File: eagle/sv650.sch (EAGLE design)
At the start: 31 parts, among them Q1 IRLML6344

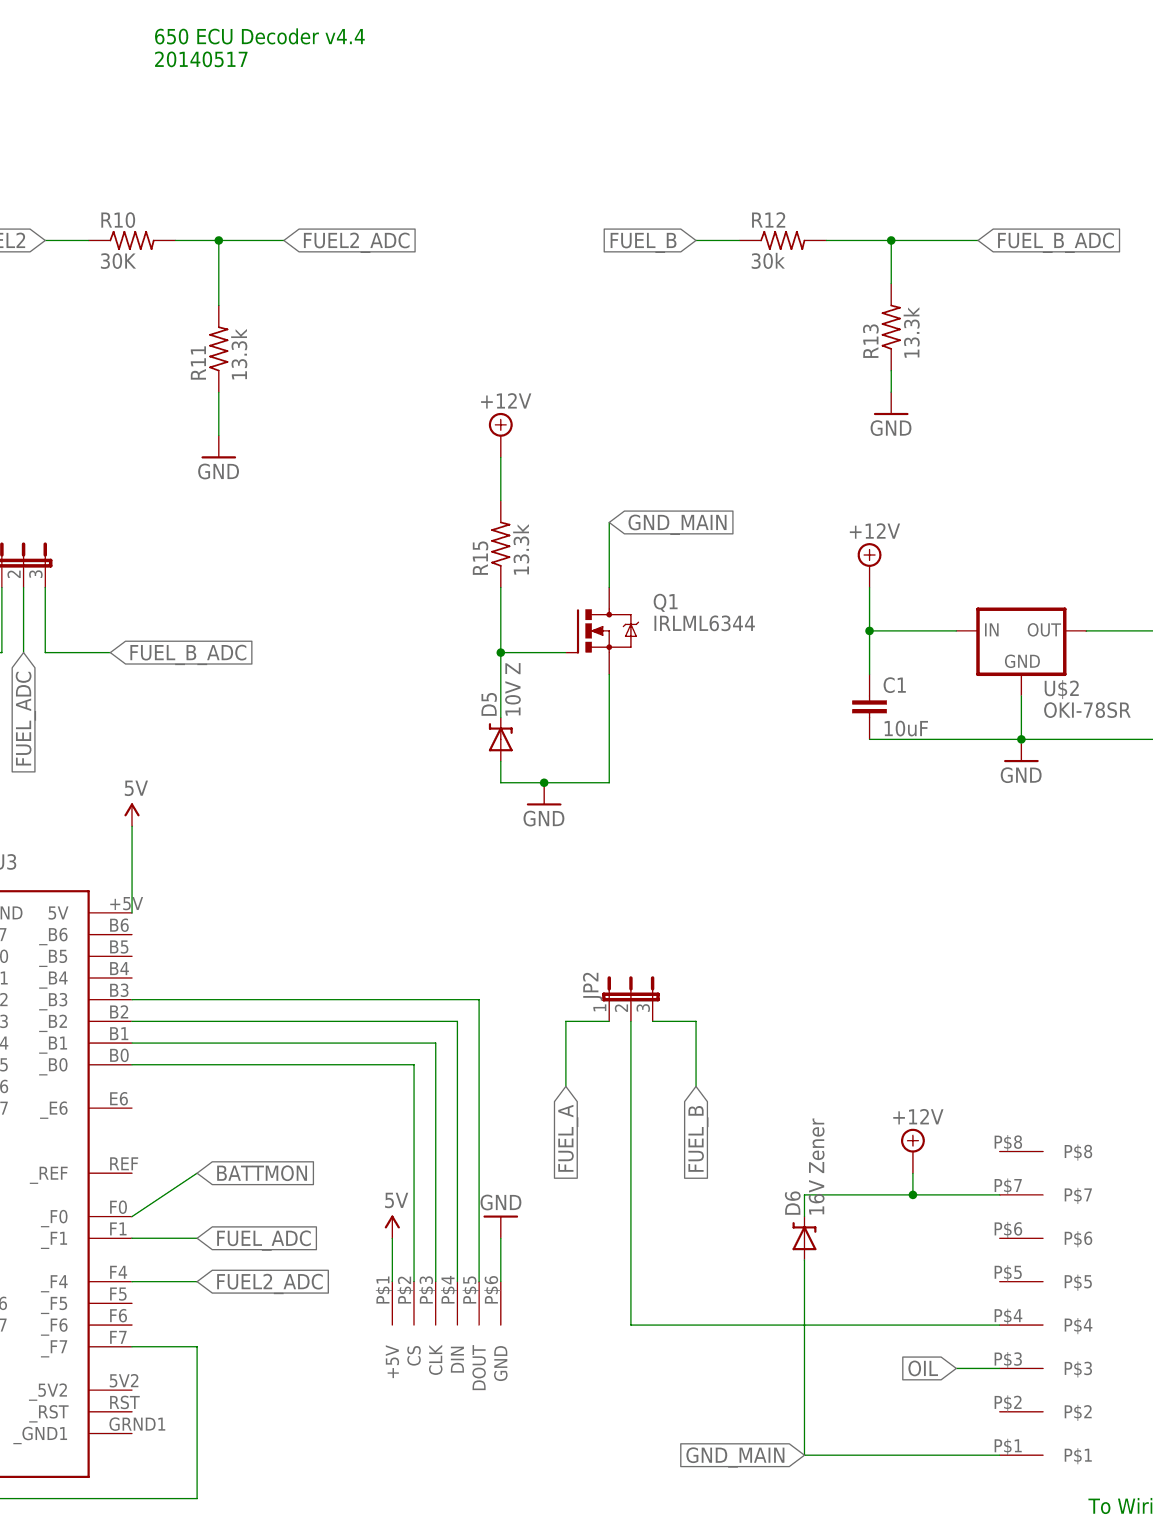
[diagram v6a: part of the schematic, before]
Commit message: replace 16V zener with 15V TVS
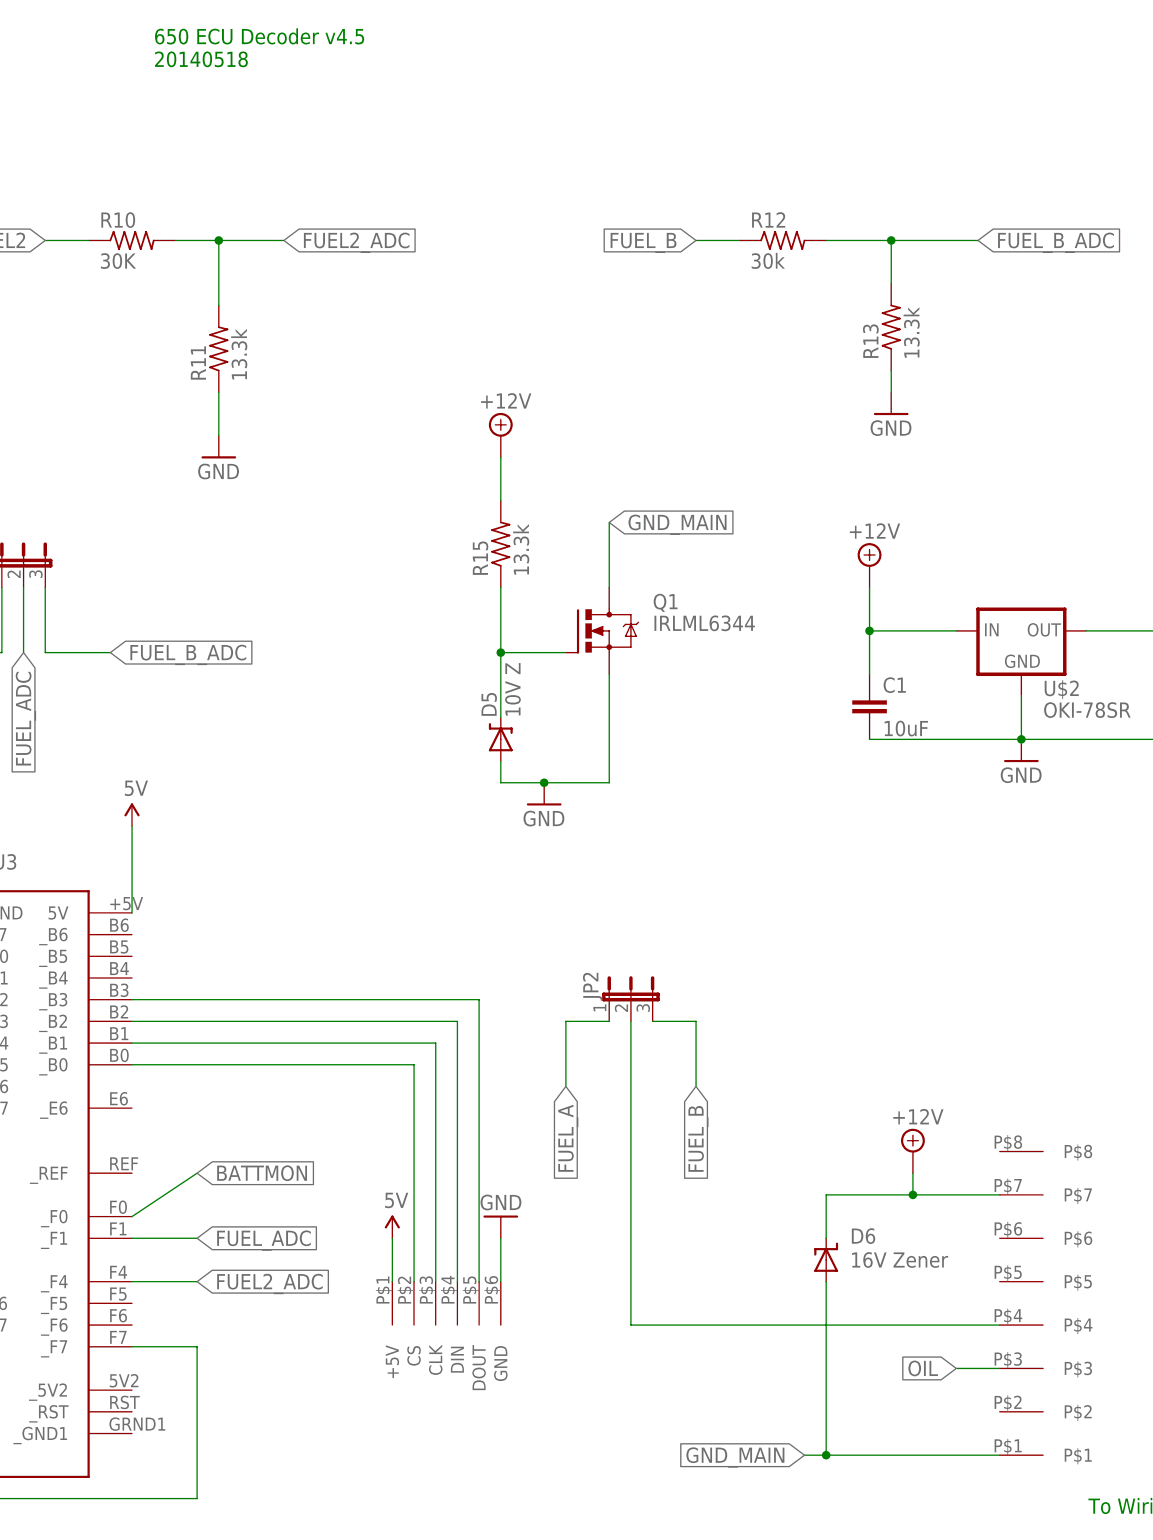
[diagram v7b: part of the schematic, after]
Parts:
- D6: device SparkFun-DiscreteSemi:DIODE-ZENER-BZT52 -> diode:SUPPRESSOR-SMBG
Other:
- note added: "650 ECU Decoder v4.5 20140518"
- note removed: "650 ECU Decoder v4.4 20140517"
- moved on the sheet: D6
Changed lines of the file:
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@@
 <part name="GND8" library="SparkFun" deviceset="GND" device=""/>
 <part name="SUPPLY1" library="supply2" deviceset="+12V" device=""/>
-<part name="D6" library="SparkFun-DiscreteSemi" deviceset="DIODE-ZENER" device="-BZT52" value="16V Zener"/>
+<part name="D6" library="diode" deviceset="SUPPRESSOR-" device="SMBG" value="16V Zener"/>
 <part name="SUPPLY3" library="supply2" deviceset="+12V" device=""/>
 <part name="R5" library="synfinatic" deviceset="RESISTOR" device="PTH-5W" value="82"/>
@@
 <plain>
 <text x="157.48" y="-38.1" size="1.778" layer="91" rot="R180">To Wiring Harness</text>
-<text x="27.94" y="129.54" size="1.778" layer="91">650 ECU Decoder v4.4
-20140517</text>
+<text x="27.94" y="129.54" size="1.778" layer="91">650 ECU Decoder v4.5
+20140518</text>
 </plain>
 <instances>
@@
 <instance part="GND8" gate="1" x="-91.44" y="15.24"/>
 <instance part="SUPPLY1" gate="+12V" x="-43.18" y="76.2"/>
-<instance part="D6" gate="G$1" x="104.14" y="-7.62" rot="R90"/>
+<instance part="D6" gate="G$1" x="106.68" y="-10.16"/>
 <instance part="SUPPLY3" gate="+12V" x="-81.28" y="129.54"/>
 <instance part="R5" gate="G$1" x="-68.58" y="116.84" rot="R90"/>
@@
 <pinref part="SUPPLY4" gate="+12V" pin="+12V"/>
 <wire x1="116.84" y1="0" x2="116.84" y2="-2.54" width="0.1524" layer="91"/>
-<wire x1="116.84" y1="-2.54" x2="104.14" y2="-2.54" width="0.1524" layer="91"/>
+<wire x1="116.84" y1="-2.54" x2="106.68" y2="-2.54" width="0.1524" layer="91"/>
 <junction x="116.84" y="-2.54"/>
-<wire x1="104.14" y1="-2.54" x2="104.14" y2="-5.08" width="0.1524" layer="91"/>
 <pinref part="D6" gate="G$1" pin="C"/>
+<wire x1="106.68" y1="-2.54" x2="106.68" y2="-7.62" width="0.1524" layer="91"/>
 </segment>
 <segment>
@@
 <segment>
 <pinref part="U$3" gate="G$1" pin="P$1"/>
-<wire x1="104.14" y1="-10.16" x2="104.14" y2="-33.02" width="0.1524" layer="91"/>
-<wire x1="104.14" y1="-33.02" x2="127" y2="-33.02" width="0.1524" layer="91"/>
+<wire x1="104.14" y1="-33.02" x2="106.68" y2="-33.02" width="0.1524" layer="91"/>
+<label x="104.14" y="-33.02" size="1.778" layer="95" rot="R180" xref="yes"/>
 <pinref part="D6" gate="G$1" pin="A"/>
-<label x="104.14" y="-33.02" size="1.778" layer="95" rot="R180" xref="yes"/>
-</segment>
-<segment>
+<wire x1="106.68" y1="-33.02" x2="127" y2="-33.02" width="0.1524" layer="91"/>
+<wire x1="106.68" y1="-12.7" x2="106.68" y2="-33.02" width="0.1524" layer="91"/>
+<junction x="106.68" y="-33.02"/>
+</segment>
+<segment>

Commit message: update to v4.6 move jumpers to back side of board
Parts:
- D6: value 16V Zener -> SMAJ15A
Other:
- note added: "650 ECU Decoder v4.6 20140517"
- note removed: "650 ECU Decoder v4.5 20140518"
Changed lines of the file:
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@@
 <part name="GND8" library="SparkFun" deviceset="GND" device=""/>
 <part name="SUPPLY1" library="supply2" deviceset="+12V" device=""/>
-<part name="D6" library="diode" deviceset="SUPPRESSOR-" device="SMBG" value="16V Zener"/>
+<part name="D6" library="diode" deviceset="SUPPRESSOR-" device="SMBG" value="SMAJ15A"/>
 <part name="SUPPLY3" library="supply2" deviceset="+12V" device=""/>
 <part name="R5" library="synfinatic" deviceset="RESISTOR" device="PTH-5W" value="82"/>
@@
 <plain>
 <text x="157.48" y="-38.1" size="1.778" layer="91" rot="R180">To Wiring Harness</text>
-<text x="27.94" y="129.54" size="1.778" layer="91">650 ECU Decoder v4.5
-20140518</text>
+<text x="27.94" y="129.54" size="1.778" layer="91">650 ECU Decoder v4.6
+20140517</text>
 </plain>
 <instances>
